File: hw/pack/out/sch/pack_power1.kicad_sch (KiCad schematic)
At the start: 20 parts, among them Q1 DMG2305UX, SW1 recessed slide, U4 TPS61023, U5 TLV75533P, U6 TLV75533P

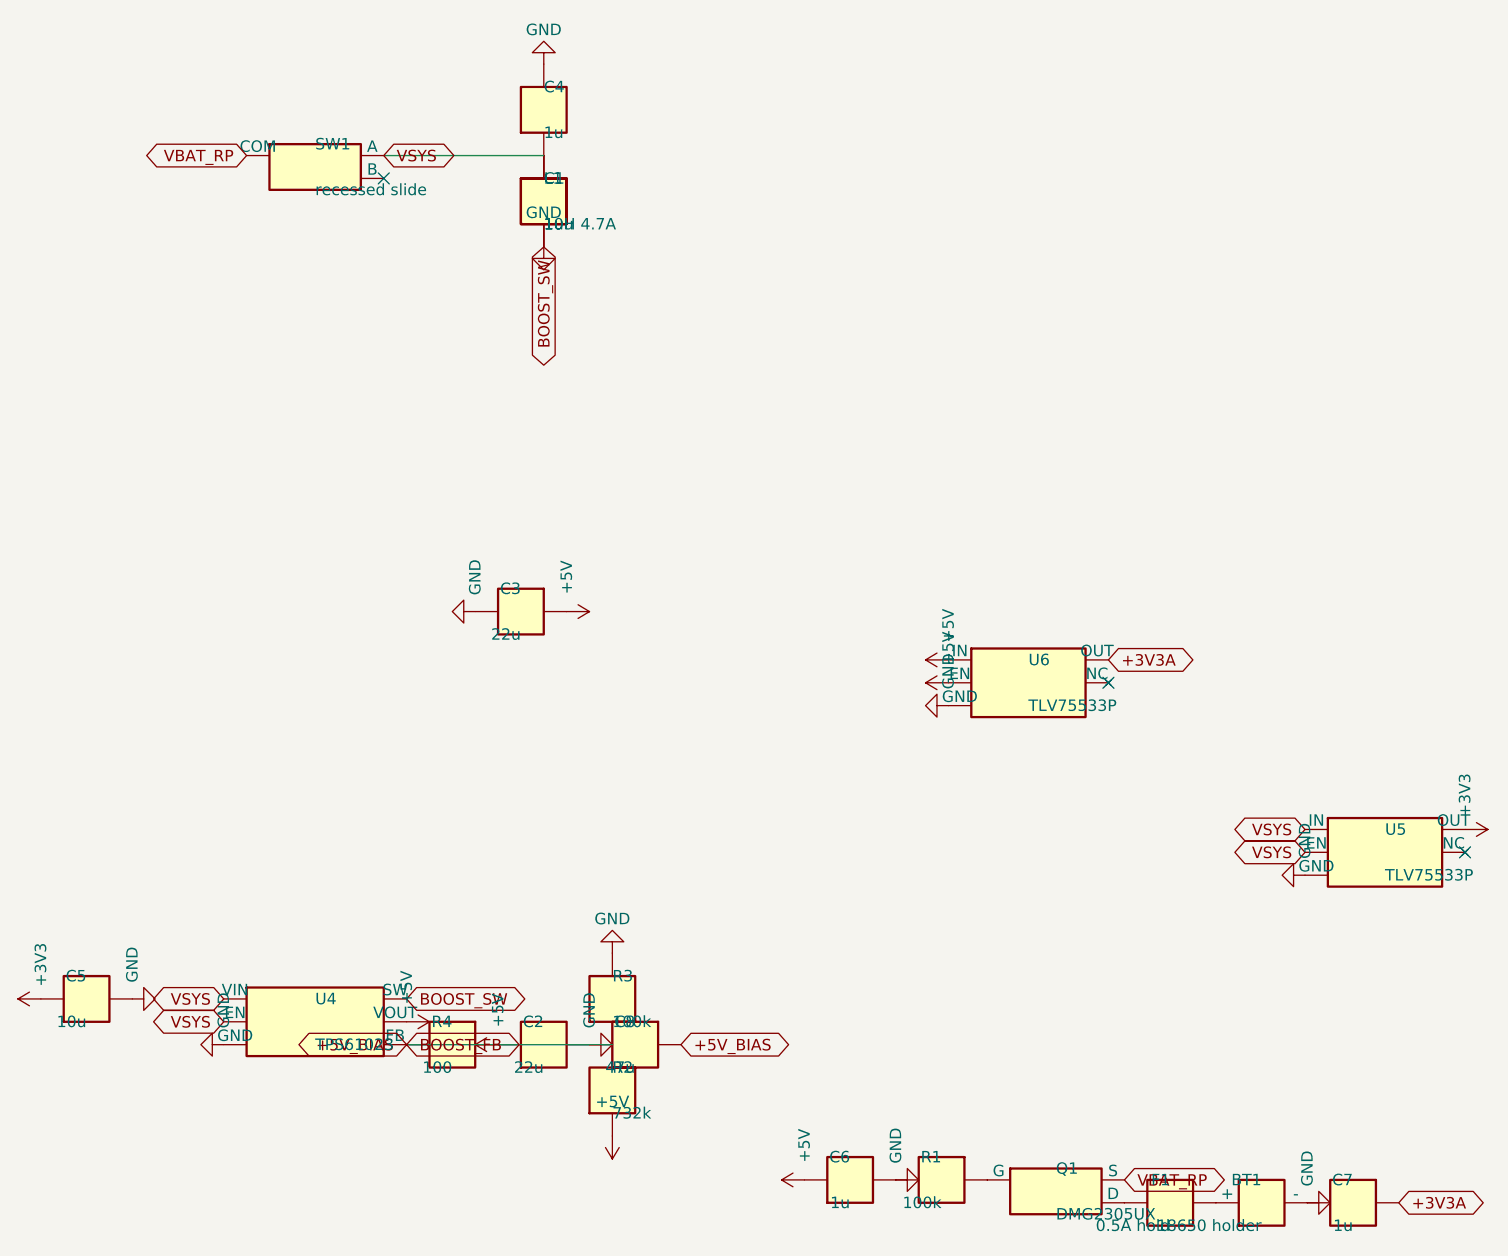
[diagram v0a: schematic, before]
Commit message: hw/pack: review fixes for #75 (op-amp CM, hot-plug protection, CI, cutoff, LEDs) (#31)
- VCM 180k/100k (1.77 V) keeps OPA1656 +IN inside V+ - 2.25 V; SPICE clamp 0.25/4.70 V,
  test asserts input CM, ADC pin (1.375 V) and prints numbers in CI (-rP)
- tip ESD (TPD1E10B06), BAV199 clamp + 100R ahead of the op-amp; C9 22p; noise 0.96 uV
- CI installs skidl==3.0.0, pack test fails (not skips) under CI, stale-output diff check
- no PTC; cell sensed at BAT+; firmware cutoff 3.2 V derived in audit.py; PK-8 LED
  thresholds -10/-7 dBFS; real LED MPNs; VDDH decoupling; audit prints DK-price BOM

Co-Authored-By: Claude Opus 5.5 <noreply@anthropic.com>
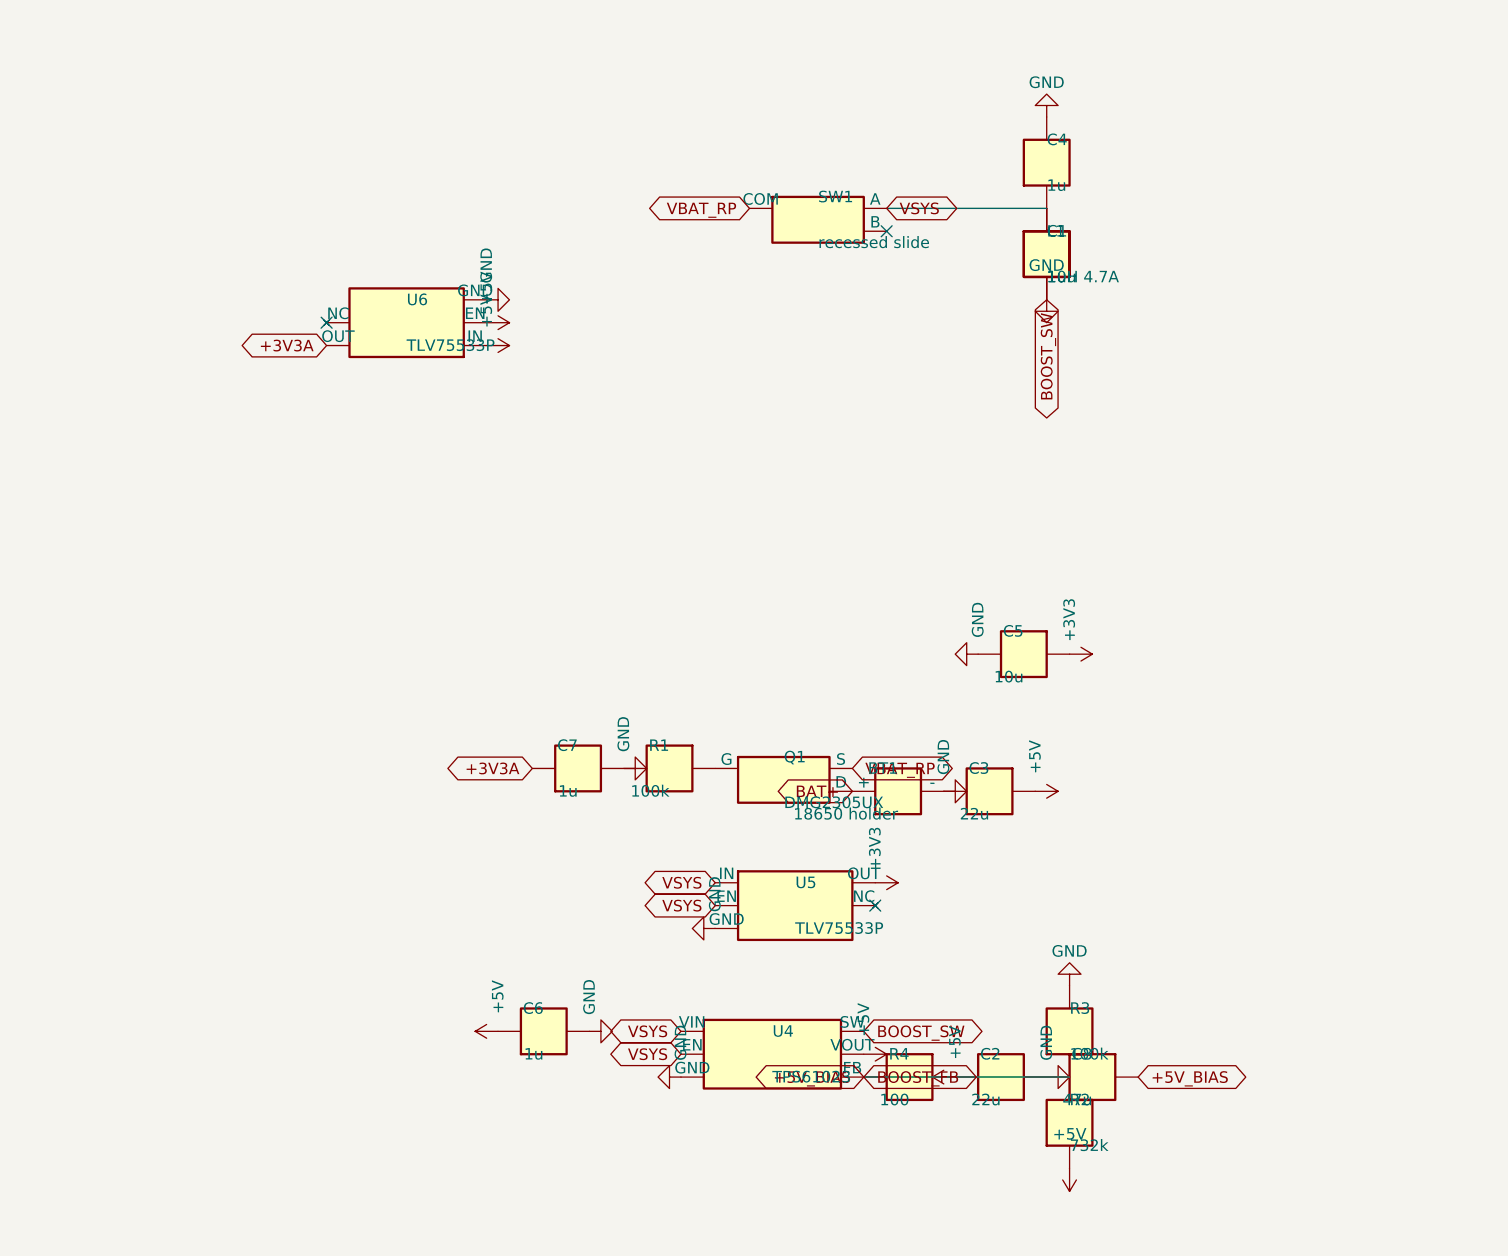
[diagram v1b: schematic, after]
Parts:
- removed F1: 0.5A hold, Fuse:Fuse_1206_3216Metric, symbol openpack:Polyfuse
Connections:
- net BAT+: now reaches BT1.1 (+)
- net BAT+: now also Q1.3 (D)
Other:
- moved on the sheet: BT1, C1, C2, C3, C4, C5, C6, C7, C8, L1, Q1, R1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

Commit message: hw/pack: 3 A chip fuse (23 mOhm) on BAT+, cutoff re-derived, BOM $34.98 (#31)
Co-Authored-By: Claude Opus 5.5 <noreply@anthropic.com>
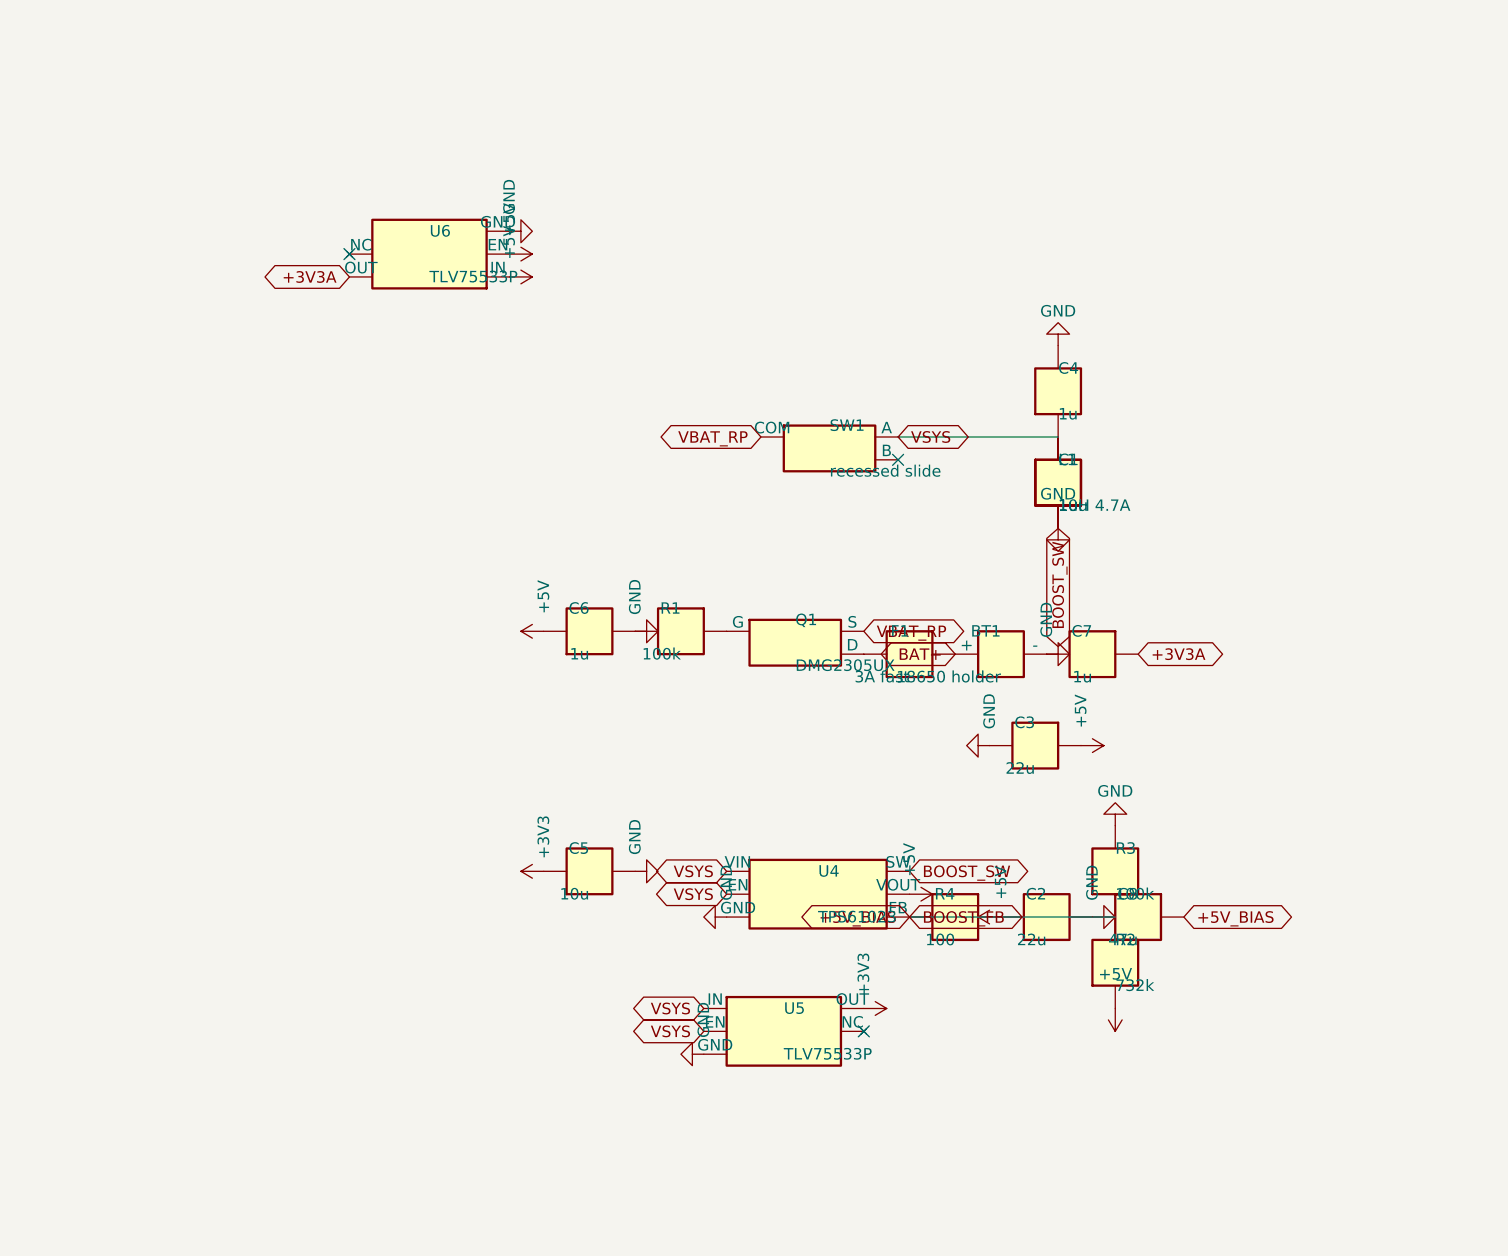
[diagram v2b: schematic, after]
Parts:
- added F1: 3A fast, Fuse:Fuse_1206_3216Metric, symbol openpack:Fuse
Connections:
- net BAT+: now also F1.1; no longer Q1.3 (D)
- new net: F1.2, Q1.3 (D)
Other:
- moved on the sheet: BT1, C1, C2, C3, C4, C5, C6, C7, C8, L1, Q1, R1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

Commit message: pack: restore battery-sense divider (R13/C30) (#84)
* hw/pack: restore battery-sense divider R13/C30 hidden in a comment

Co-Authored-By: Claude Sonnet 5.5 <noreply@anthropic.com>

* tests: cite nRF5340 SAADC pin limit (VDD) from the product spec

Co-Authored-By: Claude Sonnet 5.5 <noreply@anthropic.com>

* hw/pack: price 0402 resistors and 100n caps from LCSC qty-100 pages; UK BOM refs; merge main

Co-Authored-By: Claude Sonnet 5.5 <noreply@anthropic.com>

---------

Co-authored-by: Claude Sonnet 5.5 <noreply@anthropic.com>
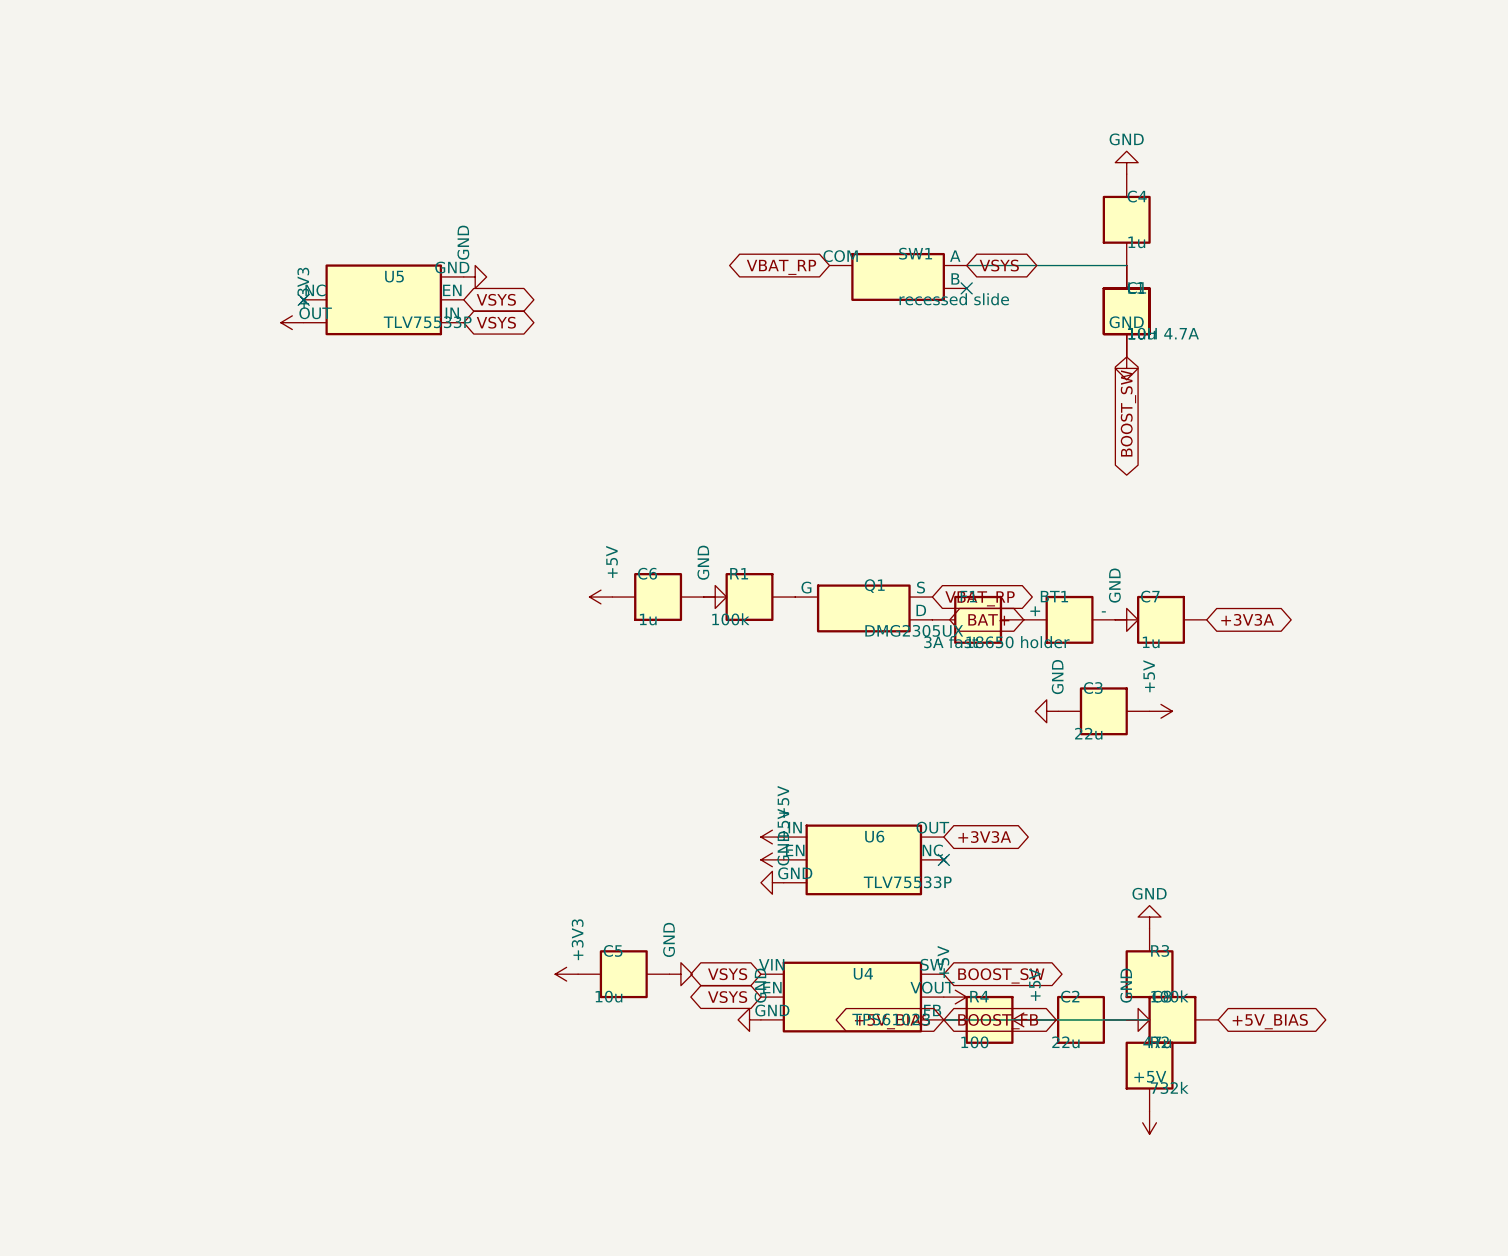
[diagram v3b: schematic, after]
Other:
- moved on the sheet: BT1, C1, C2, C3, C4, C5, C6, C7, C8, F1, L1, Q1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
